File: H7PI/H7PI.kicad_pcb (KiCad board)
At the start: 4 copper layers, 65 x 30 mm, 37 parts, among them J1 XKTF-015-N, J2 Header_2x20, J3 USBC_16P_4MP, J5 Header_2x20, U1 AMS1117-3.3, U2 LY68L6400SLIT, U3 STM32H750VBT6, U4 W25Q64JVSSIQ, U5 W25Q64JVSSIQ, X1 32.768kHz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

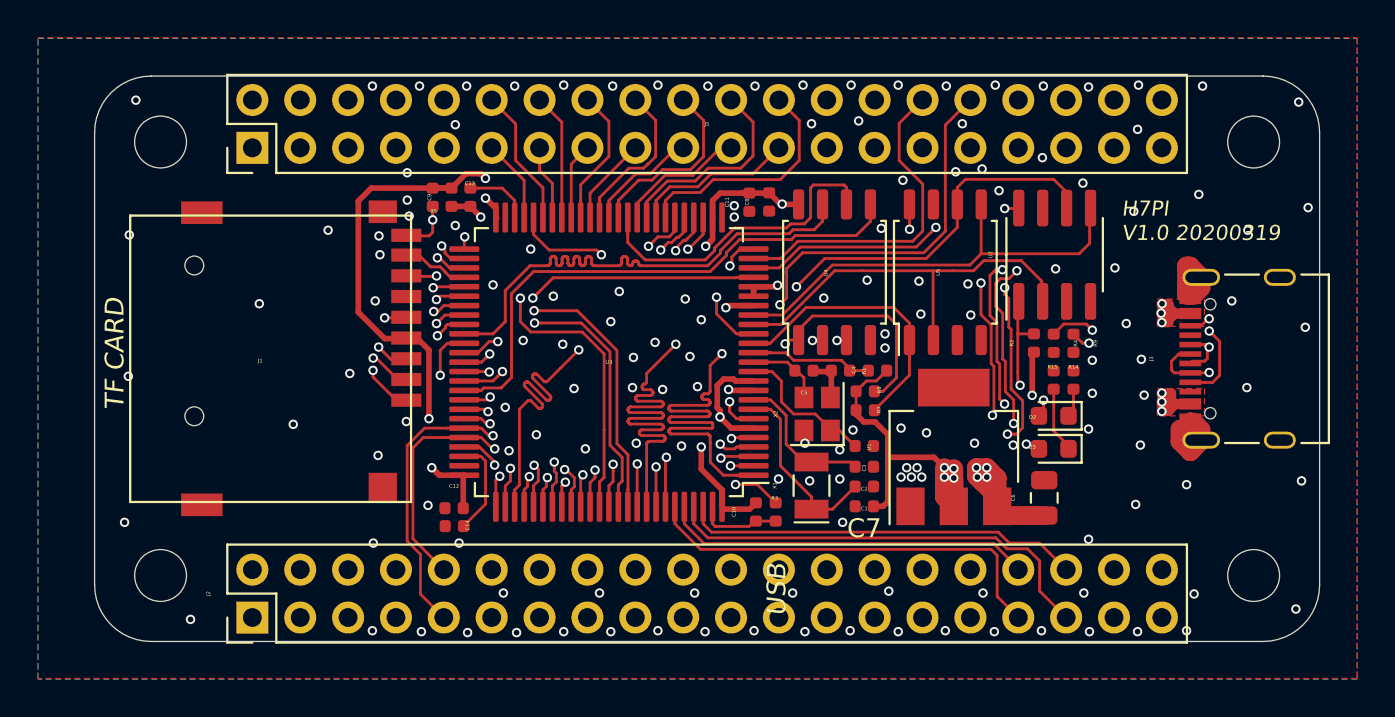
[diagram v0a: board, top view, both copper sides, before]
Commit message: v1.0第一次推送，待打样 Signed-off-by: fuhua-chen <fuhua-chen@outlook.com>
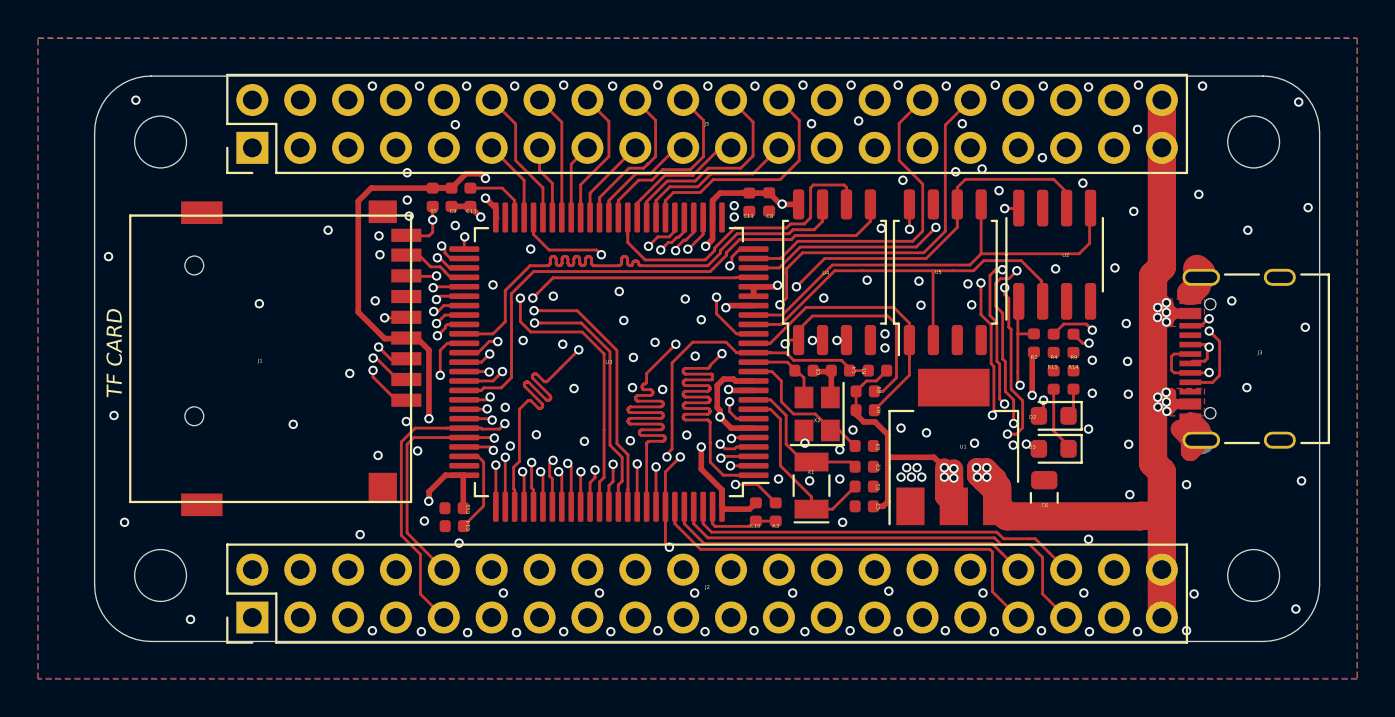
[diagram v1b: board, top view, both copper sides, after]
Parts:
- added G***: LOGO, Pinno:Pinno_Single_6.6x6.6mm, B.Cu at (191.6, 75.0)
- added G***: LOGO, Pinno:Pinno_Single_5.1x5.1mm, B.Cu at (176.6, 74.9)
- added G***: LOGO, Pinno:HTCTEK_LOGO_80, B.Cu at (145.5, 75.0)
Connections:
- J2 pad 5: (no net) -> /BOOT0
- J2 pad 6: (no net) -> /NRST
- J2 pad 7: (no net) -> /3V3
- J2 pad 8: (no net) -> /3V3
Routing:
- net /VBUS: track 70.4 -> 130.0 mm, vias 11 -> 14
- net /NRST: track 6.58 -> 37.7 mm, vias 0 -> 1
- net /BOOT0: track 9.45 -> 35.2 mm, vias 2 -> 3
- net /3V3: track 184.5 -> 194.1 mm
- net /D42: track 18.3 -> 19.6 mm
- net /D41: track 13.5 -> 14.7 mm
- net /D47: track 17.4 -> 18.3 mm
- net /QSPI_IO2: track 29.8 -> 28.9 mm
- net /D43: track 14.8 -> 15.4 mm
- net /D45: track 16.3 -> 16.9 mm
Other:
- board text added: "BOOT"
- board text added: "D24"
- board text added: "D25"
- board text added: "D26"
- board text added: "D27"
- board text added: "D28"
- board text added: "D30"
- board text added: "D31"
- board text added: "D32"
- board text added: "D33"
- board text added: "D34"
- board text added: "D35"
- board text added: "D36"
- board text added: "D37"
- board text added: "D38"
- board text added: "D39"
- board text added: "D40"
- board text added: "D41"
- board text added: "D42"
- board text added: "D43"
- board text added: "D44"
- board text added: "D45"
- board text added: "D46"
- board text added: "D47"
- board text added: "D48"
- board text added: "D49"
- board text added: "D50"
- board text added: "D51"
- board text added: "D52"
- board text added: "D53"
- board text added: "D54"
- board text added: "D55"
- board text added: "D56"
- board text added: "D57"
- board text added: "H7PI V1.0 20200320"
- board text added: "HTCTEK"
- board text added: "NRST"
- board text added: "USBN"
- board text added: "USBP"
- board text added: "pinno.cc"
- board text removed: "A0"
- board text removed: "A1"
- board text removed: "A2"
- board text removed: "A3"
- board text removed: "A4"
- board text removed: "A5"
- board text removed: "A6"
- board text removed: "A7"
- board text removed: "CE0"
- board text removed: "CE1"
- board text removed: "DN"
- board text removed: "DP"
- board text removed: "H7PI V1.0 20200319"
- board text removed: "MISO"
- board text removed: "MOSI"
- board text removed: "RX0"
- board text removed: "SCK"
- board text removed: "SCL0"
- board text removed: "SCL1"
- board text removed: "SDA0"
- board text removed: "SDA1"
- board text removed: "TX0"
- board text removed: "USB"

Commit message: 更新晶振配置 Signed-off-by: fuhua.chen <fuhua-chen@outlook.com>
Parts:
- removed G***: LOGO, Pinno:Pinno_Single_6.6x6.6mm
- removed G***: LOGO, Pinno:Pinno_Single_5.1x5.1mm
- removed G***: LOGO, Pinno:HTCTEK_LOGO_80
- C3, C5: value 8pF -> 12pF
